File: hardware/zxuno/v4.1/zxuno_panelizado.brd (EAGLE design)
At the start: 103 parts, among them T1 BC846, U1 6SLX9TQG144, U2 FLASH-SPI-25XXSMD1, U4 AD724, U5 50MHz, U6 3.3V, U7 1.2V, Y1 3.58M, Y2 4.43M

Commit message: Replico el circuito por 4 wire 0 (0 0) (190 0) (190 150) (0 150) (0 0) wire 0 (0 10) (190 10) wire 0 (0 140) (190 140)
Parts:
- added AUDIO1, AUDIO2, AUDIO3: Audio, SparkFun-Connectors:AUDIO-JACK
- added C100, C101, C107, C108, C132, C133, C134, C135, C136, C137, C143, C144, C60, C61, C62, C63, C64, C65, C71, C72, C96, C97, C98, C99: 10uF, rcl:C0805
- added C102, C103, C104, C109, C110, C111, C112, C113, C114, C115, C116, C117, C118, C119, C120, C121, C122, C123, C124, C125, C126, C127, C129, C138, C139, C140, C37, C38, C39, C40, C41, C42, C43, C44, C45, C46, C47, C48, C49, C50, C51, C52, C53, C54, C55, C57, C66, C67, C68, C73, C74, C75, C76, C77, C78, C79, C80, C81, C82, C83, C84, C85, C86, C87, C88, C89, C90, C91, C93: 100nF, rcl:C0603
- added C105, C141, C69: 7.5pF, rcl:C0805
- added C106, C142, C70: 220uF, rcl:153CLV-0605
- added C128, C130, C131, C56, C58, C59, C92, C94, C95: 10nF, rcl:C0805
- added CVBS1, CVBS2, CVBS3: RCA, uzebox:RCA
- added D10, D13, D14, D15, D18, D19, D20, D8, D9: (no value), adafruit:SOD-323F
- added D11, D12, D16, D17, D6, D7: (no value), led:CHIP-LED0805
- added EAR1, EAR2, EAR3: EAR, SparkFun-Connectors:AUDIO-JACK
- added H2, H3, H4: MOUNT-HOLE2.8, holes:2,8
- added J1, J13, J14, J2, J3, J5, J6, J7, J9: (no value), pinhead:1X12
- added J15, J4, J8: (no value), pinhead:2X02
- added JOY1, JOY2, JOY3: (no value), SparkFun-Connectors:DB9_MALE
- added JTAG1, JTAG2, JTAG3: JTAG, con-molex:53047-06
- added L10, L11, L12, L4, L5, L6, L7, L8, L9: (no value), rcl:M0805
- added PS/1, PS/3, PS/4: PS/2 Keyb, ZX_UNO_0_14:DINC/MIN_TM/6_1PRIMARY
- added PWCON1, PWCON2, PWCON3, RST1, RST2, RST3, SW1, SW2, SW3: (no value), pinhead:1X02
- added PWUSB1, PWUSB2, PWUSB3: MICROUSB, zxuno_rev_mcleod:MICRO_USB_1PRIMARY
- added R100, R104, R109, R110, R113, R116, R121, R122, R33, R34, R35, R36, R40, R45, R46, R49, R52, R57, R58, R65, R66, R67, R68, R72, R77, R78, R81, R84, R89, R90, R97, R98, R99: 510, rcl:M0805
- added R101, R106, R107, R112, R115, R118, R37, R42, R43, R48, R51, R54, R69, R74, R75, R80, R83, R86: 2K, rcl:M0805
- added R102, R103, R105, R108, R119, R120, R127, R128, R38, R39, R41, R44, R55, R56, R63, R64, R70, R71, R73, R76, R87, R88, R95, R96: 10K, rcl:M0805
- added R111, R114, R117, R47, R50, R53, R79, R82, R85: 1K, rcl:M0805
- added R123, R124, R125, R126, R59, R60, R61, R62, R91, R92, R93, R94: 75, rcl:M0805
- added RGB1, RGB2, RGB3: RGB, con-molex:53048-09
- added SDCARD1, SDCARD2, SDCARD3: (no value), zxuno_rev_mcleod:SDCMF-10915W010
- added T2, T3, T4: BC846, transistor:SOT23
- added U10, U17, U24: FLASH-SPI-25XXSMD1, GadgetFactory:SO08-EIAJ
- added U11, U18, U25: 3.3V, burr-brown:SOT223
- added U12, U19, U26: 1.2V, burr-brown:SOT223
- added U13, U20, U27: AD724, ad725:SO16W
- added U14, U21, U28: 50MHz, ZX_UNO_0_15:SM/OSC_1PRIMARY
- added U15, U22, U8: 6SLX9TQG144, xilinx_devices_V6:TQ144
- added U16, U23, U9: (no value), GadgetFactory:TSOP44-II
- added Y3, Y5, Y7: 3.58M, crystal:HC49UP
- added Y4, Y6, Y8: 4.43M, crystal:HC49UP
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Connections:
- new net 1.2V1: C39.2, C40.2, C41.2, C42.2, C43.2, L6.2, U8.P128, U8.P19, U8.P28, U8.P52, U8.P89
- new net 1.2V2: C75.2, C76.2, C77.2, C78.2, C79.2, L9.2, U15.P128, U15.P19, U15.P28, U15.P52, U15.P89
- new net 1.2V3: C111.2, C112.2, C113.2, C114.2, C115.2, L12.2, U22.P128, U22.P19, U22.P28, U22.P52, U22.P89
- new net 3.3V1: C37.1, C38.2, C44.2, C45.2, C46.2, C47.2, C48.2, C49.2, C50.2, C51.2, C52.2, C53.2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
- new net 3.3V2: C73.1, C74.2, C80.2, C81.2, C82.2, C83.2, C84.2, C85.2, C86.2, C87.2, C88.2, C89.2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
- new net 3.3V3: C109.1, C110.2, C116.2, C117.2, C118.2, C119.2, C120.2, C121.2, C122.2, C123.2, C124.2, C125.2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
- new net 5V1: C62.1, C64.1, C71.2, C72.2, J1.1, L4.2, PS/1.4, R45.1, R58.2, U11.3, U12.3, U13.14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
- new net 5V2: C100.1, C107.2, C108.2, C98.1, J5.1, L7.2, PS/3.4, R77.1, R90.2, U18.3, U19.3, U20.14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
- new net 5V3: C134.1, C136.1, C143.2, C144.2, J9.1, L10.2, PS/4.4, R109.1, R122.2, U25.3, U26.3, U27.14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
- new net AUDIO_LEFT1: R42.2, U8.P10
- new net AUDIO_LEFT2: R74.2, U15.P10
- new net AUDIO_LEFT3: R106.2, U22.P10
- new net AUDIO_RIGHT1: R43.2, U8.P9
- new net AUDIO_RIGHT2: R75.2, U15.P9
- new net AUDIO_RIGHT3: R107.2, U22.P9
- new net B10: C104.2, R84.1, R85.1, R86.1, R93.1, RGB2.7
- new net B11: R118.2, U22.P88
- new net B12: R117.2, U22.P92
- new net B13: R116.2, U22.P93
- new net B14: C140.2, R116.1, R117.1, R118.1, R125.1, RGB3.7
- new net B3: R54.2, U8.P88
- new net B4: R53.2, U8.P92
- new net B5: R52.2, U8.P93
- new net B6: C68.2, R52.1, R53.1, R54.1, R61.1, RGB1.7
- new net B7: R86.2, U15.P88
- new net B8: R85.2, U15.P92
- new net B9: R84.2, U15.P93
- new net CLK1: U14.3, U8.P55
- new net CLK2: U15.P55, U21.3
- new net CLK3: U22.P55, U28.3
- new net CSYNC1: RGB1.3, U13.16, U8.P87
- new net CSYNC2: RGB2.3, U15.P87, U20.16
- new net CSYNC3: RGB3.3, U22.P87, U27.16
- new net EAR1: R38.1, T2.3, U8.P94
- new net EAR2: R70.1, T3.3, U15.P94
- new net EAR3: R102.1, T4.3, U22.P94
- new net EXT1: J1.2, U8.P57
- new net EXT100: J9.5, U22.P43
- new net EXT101: J13.5, U22.P41
- new net EXT102: J14.5, U22.P40
- new net EXT103: J9.6, U22.P35
- new net EXT104: J13.6, U22.P34
- new net EXT105: J14.6, U22.P33
- new net EXT106: J9.7, U22.P32
- new net EXT107: J13.7, U22.P30
- new net EXT108: J14.7, U22.P29
- new net EXT109: J9.8, U22.P27
- new net EXT110: J13.8, U22.P26
- new net EXT111: J14.8, U22.P24
- new net EXT112: J9.9, U22.P23
- new net EXT113: J13.9, U22.P22
- new net EXT114: J14.9, U22.P21
- new net EXT115: J9.10, U22.P17
- new net EXT116: J13.10, U22.P16
- new net EXT117: J14.10, U22.P15
- new net EXT118: J9.11, U22.P14
- new net EXT119: J13.11, U22.P12
- new net EXT120: J14.1, U22.P58
- new net EXT2: J2.2, U8.P56
- new net EXT3: J3.2, U8.P51
- new net EXT36: J3.3, U8.P47
- new net EXT37: J1.4, U8.P46
- new net EXT38: J2.4, U8.P45
- new net EXT39: J3.4, U8.P44
- new net EXT4: J1.3, U8.P50
- new net EXT40: J1.5, U8.P43
- new net EXT41: J2.5, U8.P41
- new net EXT42: J3.5, U8.P40
- new net EXT43: J1.6, U8.P35
- new net EXT44: J2.6, U8.P34
- new net EXT45: J3.6, U8.P33
- new net EXT46: J1.7, U8.P32
- new net EXT47: J2.7, U8.P30
- new net EXT48: J3.7, U8.P29
- new net EXT49: J1.8, U8.P27
- new net EXT5: J2.3, U8.P48
- new net EXT50: J2.8, U8.P26
- new net EXT51: J3.8, U8.P24
- new net EXT52: J1.9, U8.P23
- new net EXT53: J2.9, U8.P22
- new net EXT54: J3.9, U8.P21
- new net EXT55: J1.10, U8.P17
- new net EXT56: J2.10, U8.P16
- new net EXT57: J3.10, U8.P15
- new net EXT58: J1.11, U8.P14
- new net EXT59: J2.11, U8.P12
- new net EXT60: J3.1, U8.P58
- new net EXT61: J5.2, U15.P57
- new net EXT62: J6.2, U15.P56
- new net EXT63: J7.2, U15.P51
- new net EXT64: J5.3, U15.P50
- new net EXT65: J6.3, U15.P48
- new net EXT66: J7.3, U15.P47
- new net EXT67: J5.4, U15.P46
- new net EXT68: J6.4, U15.P45
- new net EXT69: J7.4, U15.P44
- new net EXT70: J5.5, U15.P43
- new net EXT71: J6.5, U15.P41
- new net EXT72: J7.5, U15.P40
- new net EXT73: J5.6, U15.P35
- new net EXT74: J6.6, U15.P34
- new net EXT75: J7.6, U15.P33
- new net EXT76: J5.7, U15.P32
- new net EXT77: J6.7, U15.P30
- new net EXT78: J7.7, U15.P29
- new net EXT79: J5.8, U15.P27
- new net EXT80: J6.8, U15.P26
- new net EXT81: J7.8, U15.P24
- new net EXT82: J5.9, U15.P23
- new net EXT83: J6.9, U15.P22
- new net EXT84: J7.9, U15.P21
- new net EXT85: J5.10, U15.P17
- new net EXT86: J6.10, U15.P16
- new net EXT87: J7.10, U15.P15
- new net EXT88: J5.11, U15.P14
- new net EXT89: J6.11, U15.P12
- new net EXT90: J7.1, U15.P58
- new net EXT91: J9.2, U22.P57
- new net EXT92: J13.2, U22.P56
- new net EXT93: J14.2, U22.P51
- new net EXT94: J9.3, U22.P50
- new net EXT95: J13.3, U22.P48
- new net EXT96: J14.3, U22.P47
- new net EXT97: J9.4, U22.P46
- new net EXT98: J13.4, U22.P45
- new net EXT99: J14.4, U22.P44
- new net FLASH_CS1: U10.1, U8.P38
- new net FLASH_CS2: U15.P38, U17.1
- new net FLASH_CS3: U22.P38, U24.1
- new net FLASH_HOLD1: U10.7, U8.P61
- new net FLASH_HOLD2: U15.P61, U17.7
- new net FLASH_HOLD3: U22.P61, U24.7
- new net FLASH_MISO1: U10.2, U8.P65
- new net FLASH_MISO2: U15.P65, U17.2
- new net FLASH_MISO3: U22.P65, U24.2
- new net FLASH_MOSI1: U10.5, U8.P64
- new net FLASH_MOSI2: U15.P64, U17.5
- new net FLASH_MOSI3: U22.P64, U24.5
- new net FLASH_SCK1: U10.6, U8.P70
- new net FLASH_SCK2: U15.P70, U17.6
- new net FLASH_SCK3: U22.P70, U24.6
- new net FLASH_WP1: U10.3, U8.P62
- new net FLASH_WP2: U15.P62, U17.3
- new net FLASH_WP3: U22.P62, U24.3
- new net G10: C103.2, R81.1, R82.1, R83.1, R92.1, RGB2.6
- new net G11: R115.2, U22.P82
- new net G12: R114.2, U22.P83
- new net G13: R113.2, U22.P84
- new net G14: C139.2, R113.1, R114.1, R115.1, R124.1, RGB3.6
- new net G3: R51.2, U8.P82
- new net G4: R50.2, U8.P83
- new net G5: R49.2, U8.P84
- new net G6: C67.2, R49.1, R50.1, R51.1, R60.1, RGB1.6
- new net G7: R83.2, U15.P82
- new net G8: R82.2, U15.P83
- new net G9: R81.2, U15.P84
- new net GND1: AUDIO1.SLEEVE, C37.2, C38.1, C39.1, C40.1, C41.1, C42.1, C43.1, C44.1, C45.1, C46.1, C47.1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
- new net GND2: AUDIO2.SLEEVE, C100.2, C101.2, C105.2, C107.1, C108.1, C73.2, C74.1, C75.1, C76.1, C77.1, C78.1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
- new net GND3: AUDIO3.SLEEVE, C109.2, C110.1, C111.1, C112.1, C113.1, C114.1, C115.1, C116.1, C117.1, C118.1, C119.1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
- new net JOY_DOWN1: JOY1.2, U8.P5
- new net JOY_DOWN2: JOY2.2, U15.P5
- new net JOY_DOWN3: JOY3.2, U22.P5
- new net JOY_FIRE10: JOY3.6, U22.P2
- new net JOY_FIRE11: JOY3.9, U22.P8
- new net JOY_FIRE12: J15.1, U22.P39
- new net JOY_FIRE4: JOY1.6, U8.P2
- new net JOY_FIRE5: JOY1.9, U8.P8
- new net JOY_FIRE6: J4.1, U8.P39
- new net JOY_FIRE7: JOY2.6, U15.P2
- new net JOY_FIRE8: JOY2.9, U15.P8
- new net JOY_FIRE9: J8.1, U15.P39
- new net JOY_LEFT1: JOY1.3, U8.P6
- new net JOY_LEFT2: JOY2.3, U15.P6
- new net JOY_LEFT3: JOY3.3, U22.P6
- new net JOY_RIGHT1: JOY1.4, U8.P7
- new net JOY_RIGHT2: JOY2.4, U15.P7
- new net JOY_RIGHT3: JOY3.4, U22.P7
- new net JOY_UP1: JOY1.1, U8.P1
- new net JOY_UP2: JOY2.1, U15.P1
- new net JOY_UP3: JOY3.1, U22.P1
- new net L-OUT1: AUDIO1.TIP, C60.2, RGB1.9
- new net L-OUT2: AUDIO2.TIP, C96.2, RGB2.9
- new net L-OUT3: AUDIO3.TIP, C132.2, RGB3.9
- new net LED1: R57.2, U8.P11
- new net LED2: R89.2, U15.P11
- new net LED3: R121.2, U22.P11
- new net N$100: C135.1, L11.1, U25.2
- new net N$101: C137.1, L12.1, U26.2
- new net N$102: C139.1, U27.7
- new net N$103: C138.1, U27.6
- new net N$104: C141.1, U27.3, Y7.2, Y8.2
- new net N$105: D20.A, R120.1, Y8.1
- new net N$106: D19.A, R119.2, Y7.1
- new net N$107: C142.+, U27.10
- new net N$108: C140.1, U27.8
- new net N$109: C142.-, R126.1
- new net N$110: CVBS3.SIG, R126.2
- new net N$111: D16.A, R121.1
- new net N$112: D17.A, R122.1
- new net N$113: R101.1, RST3.2, U22.P37
- new net N$114: R127.1, SDCARD3.8
- new net N$115: R128.1, SDCARD3.9
- new net N$116: J15.4, R109.2
- new net N$16: PS/1.6, R33.1
- new net N$29: PS/1.5, R34.1
- new net N$30: PS/1.2, R35.1
- new net N$33: PS/1.1, R36.1
- new net N$34: R39.2, T2.1
- new net N$35: C56.1, C57.1, D8.C, R39.1
- new net N$36: C57.2, R40.2
- new net N$37: EAR1.TIP, R40.1, R41.1
- new net N$38: C58.1, C61.1, R43.1
- new net N$39: C59.1, C60.1, R42.1
- new net N$40: PWCON1.2, PWUSB1.1, SW1.2
- new net N$41: L4.1, SW1.1
- new net N$42: C63.1, L5.1, U11.2
- new net N$43: C65.1, L6.1, U12.2
- new net N$44: C67.1, U13.7
- new net N$45: C66.1, U13.6
- new net N$46: C69.1, U13.3, Y3.2, Y4.2
- new net N$47: D10.A, R56.1, Y4.1
- new net N$48: D9.A, R55.2, Y3.1
- new net N$49: C70.+, U13.10
- new net N$50: C68.1, U13.8
- new net N$51: C70.-, R62.1
- new net N$52: CVBS1.SIG, R62.2
- new net N$53: D6.A, R57.1
- new net N$54: D7.A, R58.1
- new net N$55: R37.1, RST1.2, U8.P37
- new net N$56: R63.1, SDCARD1.8
- new net N$57: R64.1, SDCARD1.9
- new net N$58: J4.4, R45.2
- new net N$59: PS/3.6, R65.1
- new net N$60: PS/3.5, R66.1
- new net N$61: PS/3.2, R67.1
- new net N$62: PS/3.1, R68.1
- new net N$63: R71.2, T3.1
- new net N$64: C92.1, C93.1, D13.C, R71.1
- new net N$65: C93.2, R72.2
- new net N$66: EAR2.TIP, R72.1, R73.1
- new net N$67: C94.1, C97.1, R75.1
- new net N$68: C95.1, C96.1, R74.1
- new net N$69: PWCON2.2, PWUSB2.1, SW2.2
- new net N$70: L7.1, SW2.1
- new net N$71: C99.1, L8.1, U18.2
- new net N$72: C101.1, L9.1, U19.2
- new net N$73: C103.1, U20.7
- new net N$74: C102.1, U20.6
- new net N$75: C105.1, U20.3, Y5.2, Y6.2
- new net N$76: D15.A, R88.1, Y6.1
- new net N$77: D14.A, R87.2, Y5.1
- new net N$78: C106.+, U20.10
- new net N$79: C104.1, U20.8
- new net N$80: C106.-, R94.1
- new net N$81: CVBS2.SIG, R94.2
- new net N$82: D11.A, R89.1
- new net N$83: D12.A, R90.1
- new net N$84: R69.1, RST2.2, U15.P37
- new net N$85: R95.1, SDCARD2.8
- new net N$86: R96.1, SDCARD2.9
- new net N$87: J8.4, R77.2
- new net N$88: PS/4.6, R97.1
- new net N$89: PS/4.5, R98.1
- new net N$90: PS/4.2, R99.1
- new net N$91: PS/4.1, R100.1
- new net N$92: R103.2, T4.1
- new net N$93: C128.1, C129.1, D18.C, R103.1
- new net N$94: C129.2, R104.2
- new net N$95: EAR3.TIP, R104.1, R105.1
- new net N$96: C130.1, C133.1, R107.1
- new net N$97: C131.1, C132.1, R106.1
- new net N$98: PWCON3.2, PWUSB3.1, SW3.2
- new net N$99: L10.1, SW3.1
- new net PIN1: J4.3, JOY1.7
- new net PIN2: J4.2, JOY1.5
- new net PIN3: J8.3, JOY2.7
- new net PIN4: J8.2, JOY2.5
- new net PIN6: J15.3, JOY3.7
- new net PIN8: J15.2, JOY3.5
- new net PS2_CLK1: R34.2, U8.P99
- new net PS2_CLK2: R66.2, U15.P99
- new net PS2_CLK3: R98.2, U22.P99
- new net PS2_DATA1: R36.2, U8.P98
- new net PS2_DATA2: R68.2, U15.P98
- new net PS2_DATA3: R100.2, U22.P98
- new net PS2_PIN1: R33.2, U8.P95
- new net PS2_PIN3: R35.2, U8.P97
- new net PS2_PIN4: R65.2, U15.P95
- new net PS2_PIN5: R67.2, U15.P97
- new net PS2_PIN7: R97.2, U22.P95
- new net PS2_PIN8: R99.2, U22.P97
- new net R-OUT1: AUDIO1.RING, C61.2, RGB1.8
- new net R-OUT2: AUDIO2.RING, C97.2, RGB2.8
- new net R-OUT3: AUDIO3.RING, C133.2, RGB3.8
- new net R10: C102.2, R78.1, R79.1, R80.1, R91.1, RGB2.5
- new net R11: R112.2, U22.P79
- new net R12: R111.2, U22.P80
- new net R13: R110.2, U22.P81
- new net R14: C138.2, R110.1, R111.1, R112.1, R123.1, RGB3.5
- new net R3: R48.2, U8.P79
- new net R4: R47.2, U8.P80
- new net R5: R46.2, U8.P81
- new net R6: C66.2, R46.1, R47.1, R48.1, R59.1, RGB1.5
- new net R7: R80.2, U15.P79
- new net R8: R79.2, U15.P80
- new net R9: R78.2, U15.P81
- new net SD_CS1: SDCARD1.1, U8.P59
- new net SD_CS2: SDCARD2.1, U15.P59
- new net SD_CS3: SDCARD3.1, U22.P59
- new net SD_MISO1: R44.2, SDCARD1.7, U8.P78
- new net SD_MISO2: R76.2, SDCARD2.7, U15.P78
- new net SD_MISO3: R108.2, SDCARD3.7, U22.P78
- new net SD_MOSI1: SDCARD1.2, U8.P74
- new net SD_MOSI2: SDCARD2.2, U15.P74
- new net SD_MOSI3: SDCARD3.2, U22.P74
- new net SD_SCK1: SDCARD1.5, U8.P75
- new net SD_SCK2: SDCARD2.5, U15.P75
- new net SD_SCK3: SDCARD3.5, U22.P75
- new net STDN1: R55.1, U13.1, U8.P66
- new net STDN2: R87.1, U15.P66, U20.1
- new net STDN3: R119.1, U22.P66, U27.1
- new net STDNB1: R56.2, U8.P67
- new net STDNB2: R88.2, U15.P67
- new net STDNB3: R120.2, U22.P67
- new net TCK1: JTAG1.3, U8.P109
- new net TCK2: JTAG2.3, U15.P109
- new net TCK3: JTAG3.3, U22.P109
- new net TDI1: JTAG1.5, U8.P110
- new net TDI2: JTAG2.5, U15.P110
- new net TDI3: JTAG3.5, U22.P110
- new net TDO1: JTAG1.4, U8.P106
- new net TDO2: JTAG2.4, U15.P106
- new net TDO3: JTAG3.4, U22.P106
- new net TMS1: JTAG1.6, U8.P107
- new net TMS2: JTAG2.6, U15.P107
- new net TMS3: JTAG3.6, U22.P107
- new net VSYNC1: RGB1.2, U8.P85
- new net VSYNC2: RGB2.2, U15.P85
- new net VSYNC3: RGB3.2, U22.P85
- new net WR1: U8.P121, U9.15
- new net WR2: U15.P121, U16.15
- new net WR3: U22.P121, U23.15
- new net XA21: U8.P141, U9.3
- new net XA22: U8.P137, U9.5
- new net XA23: U8.P134, U9.6
- new net XA24: U8.P133, U9.7
- new net XA25: U8.P120, U9.16
- new net XA26: U8.P118, U9.17
- new net XA27: U8.P116, U9.18
- new net XA28: U8.P114, U9.19
- new net XA29: U8.P112, U9.20
- new net XA30: U8.P104, U9.26
- new net XA31: U8.P102, U9.27
- new net XA32: U8.P101, U9.28
- new net XA33: U8.P100, U9.29
- new net XA34: U8.P111, U9.30
- new net XA35: U8.P131, U9.38
- new net XA36: U8.P138, U9.39
- new net XA37: U8.P140, U9.40
- new net XA38: U8.P142, U9.41
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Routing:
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- added copper zone on layer 1, net GND1
- added copper zone on layer 16, net GND1
- added copper zone on layer 1, net GND2
- added copper zone on layer 16, net GND2
- added copper zone on layer 1, net GND3
- added copper zone on layer 16, net GND3
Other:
- board outline added: 190 x 150 mm

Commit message: wire 0 (0 66) (190 66) wire 0 (0 84) (190 84) wire 0 (86 10) (86 140) wire 0 (104 10) (104 140)
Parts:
- moved AUDIO2 0.06 mm to (169.4, 136.4)
- moved D11 0.06 mm to (185.3, 138.4)
- moved H3 0.06 mm to (141.0, 136.0)
- moved J7 0.06 mm to (121.2, 138.0)
- moved R89 0.06 mm to (179.8, 138.4)
- moved C101 0.06 mm to (117.6, 108.8)
- moved C103 0.06 mm to (135.0, 96.8)
- moved C73 0.06 mm to (175.2, 114.1)
- moved C74 0.06 mm to (123.1, 111.0)
- moved C75 0.06 mm to (141.2, 123.6)
- moved C76 0.06 mm to (148.1, 123.6)
- moved C77 0.06 mm to (155.1, 115.5)
- moved C79 0.06 mm to (136.5, 117.0)
- moved C80 0.06 mm to (144.3, 123.6)
- moved C81 0.06 mm to (153.3, 123.6)
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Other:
- outline, holes or cut-outs redrawn

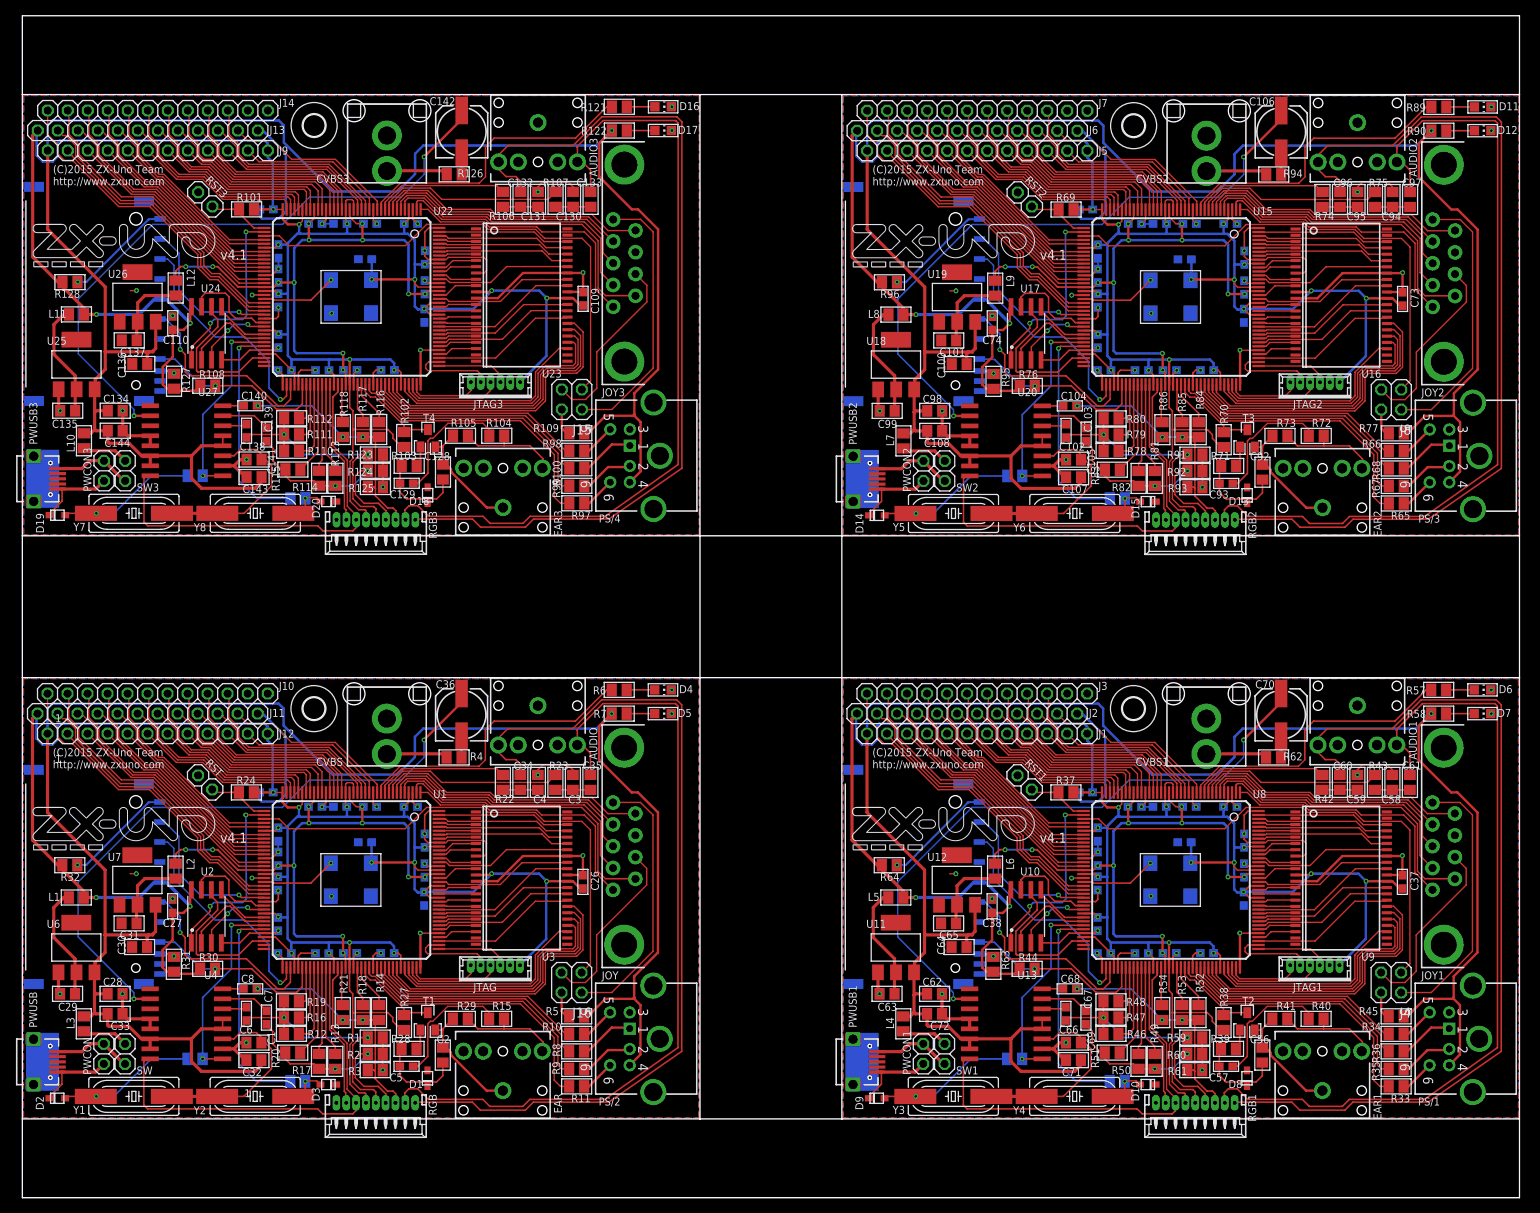
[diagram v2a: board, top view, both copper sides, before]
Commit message: Añado fiduciales y borro esquemático panelizado
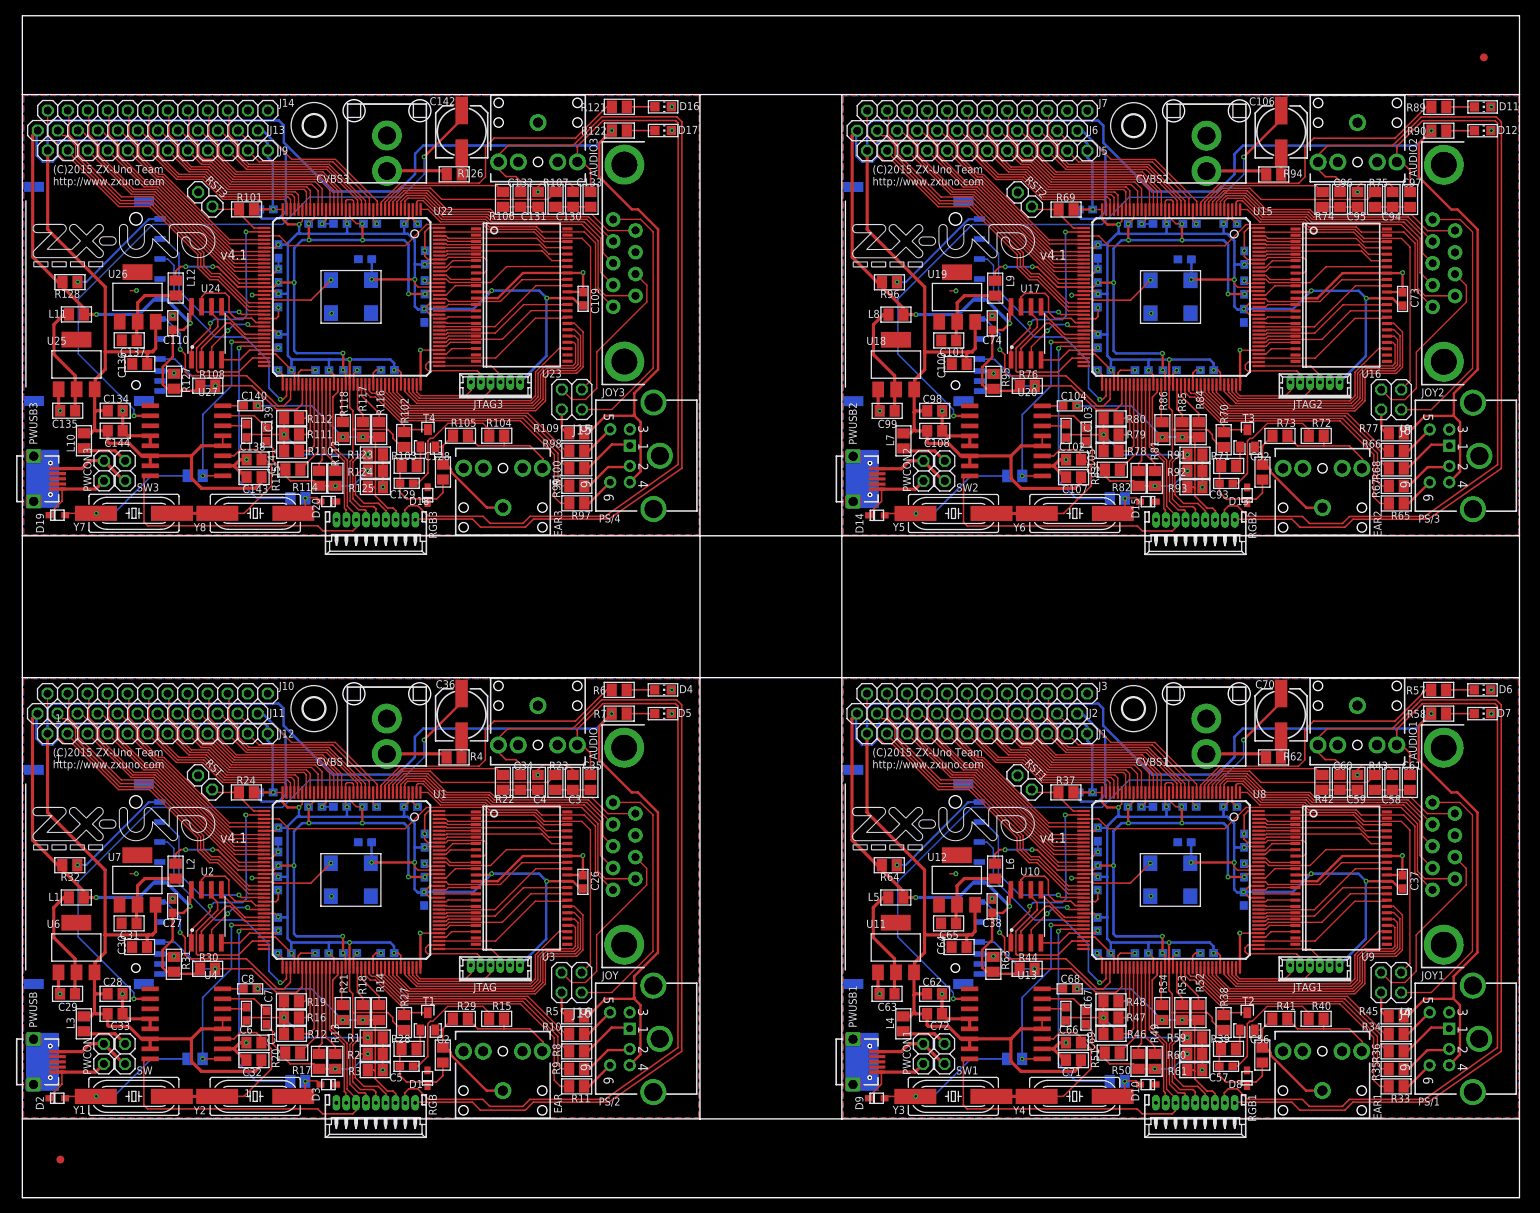
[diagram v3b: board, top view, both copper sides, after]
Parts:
- added E$1, E$2: (no value), adafruit:FIDUCIAL_1MM
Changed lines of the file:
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@@
 <attribute name="NAME" x="37.30625" y="128.80578125" size="1.016" layer="25" font="vector" ratio="15"/>
 </element>
+<element name="E$1" library="adafruit" package="FIDUCIAL_1MM" value="" x="4.82203125" y="4.841875"/>
+<element name="E$2" library="adafruit" package="FIDUCIAL_1MM" value="" x="185.47953125" y="144.72046875"/>
 </elements>
 <signals>

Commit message: Vacío panelizado
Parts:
- removed AUDIO, AUDIO1, AUDIO2, AUDIO3: Audio, SparkFun-Connectors:AUDIO-JACK
- removed C1, C105, C141, C69: 7.5pF, rcl:C0805
- removed C10, C102, C103, C104, C109, C11, C110, C111, C112, C113, C114, C115, C116, C117, C118, C119, C12, C120, C121, C122, C123, C124, C125, C126, C127, C129, C13, C138, C139, C14, C140, C15, C16, C17, C18, C19, C20, C21, C22, C23, C24, C25, C26, C27, C37, C38, C39, C40, C41, C42, C43, C44, C45, C46, C47, C48, C49, C5, C50, C51, C52, C53, C54, C55, C57, C6, C66, C67, C68, C7, C73, C74, C75, C76, C77, C78, C79, C8, C80, C81, C82, C83, C84, C85, C86, C87, C88, C89, C9, C90, C91, C93: 100nF, rcl:C0603
- removed C100, C101, C107, C108, C132, C133, C134, C135, C136, C137, C143, C144, C28, C29, C30, C31, C32, C33, C34, C35, C60, C61, C62, C63, C64, C65, C71, C72, C96, C97, C98, C99: 10uF, rcl:C0805
- removed C106, C142, C36, C70: 220uF, rcl:153CLV-0605
- removed C128, C130, C131, C2, C3, C4, C56, C58, C59, C92, C94, C95: 10nF, rcl:C0805
- removed CVBS, CVBS1, CVBS2, CVBS3: RCA, uzebox:RCA
- removed D1, D10, D13, D14, D15, D18, D19, D2, D20, D3, D8, D9: (no value), adafruit:SOD-323F
- removed D11, D12, D16, D17, D4, D5, D6, D7: (no value), led:CHIP-LED0805
- removed EAR, EAR1, EAR2, EAR3: EAR, SparkFun-Connectors:AUDIO-JACK
- removed H1, H2, H3, H4: MOUNT-HOLE2.8, holes:2,8
- removed J1, J10, J11, J12, J13, J14, J2, J3, J5, J6, J7, J9: (no value), pinhead:1X12
- removed J15, J16, J4, J8: (no value), pinhead:2X02
- removed JOY, JOY1, JOY2, JOY3: (no value), SparkFun-Connectors:DB9_MALE
- removed JTAG, JTAG1, JTAG2, JTAG3: JTAG, con-molex:53047-06
- removed L1, L10, L11, L12, L2, L3, L4, L5, L6, L7, L8, L9: (no value), rcl:M0805
- removed PS/1, PS/2, PS/3, PS/4: PS/2 Keyb, ZX_UNO_0_14:DINC/MIN_TM/6_1PRIMARY
- removed PWCON, PWCON1, PWCON2, PWCON3, RST, RST1, RST2, RST3, SW, SW1, SW2, SW3: (no value), pinhead:1X02
- removed PWUSB, PWUSB1, PWUSB2, PWUSB3: MICROUSB, zxuno_rev_mcleod:MICRO_USB_1PRIMARY
- removed R1, R123, R124, R125, R126, R2, R3, R4, R59, R60, R61, R62, R91, R92, R93, R94: 75, rcl:M0805
- removed R10, R100, R104, R109, R11, R110, R113, R116, R12, R121, R122, R13, R14, R15, R33, R34, R35, R36, R40, R45, R46, R49, R5, R52, R57, R58, R6, R65, R66, R67, R68, R7, R72, R77, R78, R8, R81, R84, R89, R9, R90, R97, R98, R99: 510, rcl:M0805
- removed R101, R106, R107, R112, R115, R118, R19, R20, R21, R22, R23, R24, R37, R42, R43, R48, R51, R54, R69, R74, R75, R80, R83, R86: 2K, rcl:M0805
- removed R102, R103, R105, R108, R119, R120, R127, R128, R25, R26, R27, R28, R29, R30, R31, R32, R38, R39, R41, R44, R55, R56, R63, R64, R70, R71, R73, R76, R87, R88, R95, R96: 10K, rcl:M0805
- removed R111, R114, R117, R16, R17, R18, R47, R50, R53, R79, R82, R85: 1K, rcl:M0805
- removed RGB, RGB1, RGB2, RGB3: RGB, con-molex:53048-09
- removed SDCARD, SDCARD1, SDCARD2, SDCARD3: (no value), zxuno_rev_mcleod:SDCMF-10915W010
- removed T1, T2, T3, T4: BC846, transistor:SOT23
- removed U1, U15, U22, U8: 6SLX9TQG144, xilinx_devices_V6:TQ144
- removed U10, U17, U2, U24: FLASH-SPI-25XXSMD1, GadgetFactory:SO08-EIAJ
- removed U11, U18, U25, U6: 3.3V, burr-brown:SOT223
- removed U12, U19, U26, U7: 1.2V, burr-brown:SOT223
- removed U13, U20, U27, U4: AD724, ad725:SO16W
- removed U14, U21, U28, U5: 50MHz, ZX_UNO_0_15:SM/OSC_1PRIMARY
- removed U16, U23, U3, U9: (no value), GadgetFactory:TSOP44-II
- removed Y1, Y3, Y5, Y7: 3.58M, crystal:HC49UP
- removed Y2, Y4, Y6, Y8: 4.43M, crystal:HC49UP
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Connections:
- removed net 1.2V: C10.2, C11.2, C12.2, C13.2, C9.2, L2.2, U1.P128, U1.P19, U1.P28, U1.P52, U1.P89
- removed net 1.2V1: C39.2, C40.2, C41.2, C42.2, C43.2, L6.2, U8.P128, U8.P19, U8.P28, U8.P52, U8.P89
- removed net 1.2V2: C75.2, C76.2, C77.2, C78.2, C79.2, L9.2, U15.P128, U15.P19, U15.P28, U15.P52, U15.P89
- removed net 1.2V3: C111.2, C112.2, C113.2, C114.2, C115.2, L12.2, U22.P128, U22.P19, U22.P28, U22.P52, U22.P89
- removed net 3.3V: C14.2, C15.2, C16.2, C17.2, C18.2, C19.2, C20.2, C21.2, C22.2, C23.2, C24.2, C25.2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
- removed net 3.3V1: C37.1, C38.2, C44.2, C45.2, C46.2, C47.2, C48.2, C49.2, C50.2, C51.2, C52.2, C53.2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
- removed net 3.3V2: C73.1, C74.2, C80.2, C81.2, C82.2, C83.2, C84.2, C85.2, C86.2, C87.2, C88.2, C89.2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
- removed net 3.3V3: C109.1, C110.2, C116.2, C117.2, C118.2, C119.2, C120.2, C121.2, C122.2, C123.2, C124.2, C125.2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
- removed net 5V: C28.1, C30.1, C32.2, C33.2, J12.1, L3.2, PS/2.4, R5.1, R7.2, U4.14, U4.15, U4.4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
- removed net 5V1: C62.1, C64.1, C71.2, C72.2, J1.1, L4.2, PS/1.4, R45.1, R58.2, U11.3, U12.3, U13.14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
- removed net 5V2: C100.1, C107.2, C108.2, C98.1, J5.1, L7.2, PS/3.4, R77.1, R90.2, U18.3, U19.3, U20.14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
- removed net 5V3: C134.1, C136.1, C143.2, C144.2, J9.1, L10.2, PS/4.4, R109.1, R122.2, U25.3, U26.3, U27.14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
- removed net AUDIO_LEFT: R22.2, U1.P10
- removed net AUDIO_LEFT1: R42.2, U8.P10
- removed net AUDIO_LEFT2: R74.2, U15.P10
- removed net AUDIO_LEFT3: R106.2, U22.P10
- removed net AUDIO_RIGHT: R23.2, U1.P9
- removed net AUDIO_RIGHT1: R43.2, U8.P9
- removed net AUDIO_RIGHT2: R75.2, U15.P9
- removed net AUDIO_RIGHT3: R107.2, U22.P9
- removed net B: C8.2, R14.1, R18.1, R21.1, R3.1, RGB.7
- removed net B0: R21.2, U1.P88
- removed net B1: R18.2, U1.P92
- removed net B10: C104.2, R84.1, R85.1, R86.1, R93.1, RGB2.7
- removed net B11: R118.2, U22.P88
- removed net B12: R117.2, U22.P92
- removed net B13: R116.2, U22.P93
- removed net B14: C140.2, R116.1, R117.1, R118.1, R125.1, RGB3.7
- removed net B2: R14.2, U1.P93
- removed net B3: R54.2, U8.P88
- removed net B4: R53.2, U8.P92
- removed net B5: R52.2, U8.P93
- removed net B6: C68.2, R52.1, R53.1, R54.1, R61.1, RGB1.7
- removed net B7: R86.2, U15.P88
- removed net B8: R85.2, U15.P92
- removed net B9: R84.2, U15.P93
- removed net CLK: U1.P55, U5.3
- removed net CLK1: U14.3, U8.P55
- removed net CLK2: U15.P55, U21.3
- removed net CLK3: U22.P55, U28.3
- removed net CSYNC: RGB.3, U1.P87, U4.16
- removed net CSYNC1: RGB1.3, U13.16, U8.P87
- removed net CSYNC2: RGB2.3, U15.P87, U20.16
- removed net CSYNC3: RGB3.3, U22.P87, U27.16
- removed net EAR: R27.1, T1.3, U1.P94
- removed net EAR1: R38.1, T2.3, U8.P94
- removed net EAR2: R70.1, T3.3, U15.P94
- removed net EAR3: R102.1, T4.3, U22.P94
- removed net EXT1: J1.2, U8.P57
- removed net EXT10: J12.3, U1.P50
- removed net EXT100: J9.5, U22.P43
- removed net EXT101: J13.5, U22.P41
- removed net EXT102: J14.5, U22.P40
- removed net EXT103: J9.6, U22.P35
- removed net EXT104: J13.6, U22.P34
- removed net EXT105: J14.6, U22.P33
- removed net EXT106: J9.7, U22.P32
- removed net EXT107: J13.7, U22.P30
- removed net EXT108: J14.7, U22.P29
- removed net EXT109: J9.8, U22.P27
- removed net EXT11: J11.3, U1.P48
- removed net EXT110: J13.8, U22.P26
- removed net EXT111: J14.8, U22.P24
- removed net EXT112: J9.9, U22.P23
- removed net EXT113: J13.9, U22.P22
- removed net EXT114: J14.9, U22.P21
- removed net EXT115: J9.10, U22.P17
- removed net EXT116: J13.10, U22.P16
- removed net EXT117: J14.10, U22.P15
- removed net EXT118: J9.11, U22.P14
- removed net EXT119: J13.11, U22.P12
- removed net EXT12: J10.3, U1.P47
- removed net EXT120: J14.1, U22.P58
- removed net EXT13: J12.4, U1.P46
- removed net EXT14: J11.4, U1.P45
- removed net EXT15: J10.4, U1.P44
- removed net EXT16: J12.5, U1.P43
- removed net EXT17: J11.5, U1.P41
- removed net EXT18: J10.5, U1.P40
- removed net EXT19: J12.6, U1.P35
- removed net EXT2: J2.2, U8.P56
- removed net EXT20: J11.6, U1.P34
- removed net EXT21: J10.6, U1.P33
- removed net EXT22: J12.7, U1.P32
- removed net EXT23: J11.7, U1.P30
- removed net EXT24: J10.7, U1.P29
- removed net EXT25: J12.8, U1.P27
- removed net EXT26: J11.8, U1.P26
- removed net EXT27: J10.8, U1.P24
- removed net EXT28: J12.9, U1.P23
- removed net EXT29: J11.9, U1.P22
- removed net EXT3: J3.2, U8.P51
- removed net EXT30: J10.9, U1.P21
- removed net EXT31: J12.10, U1.P17
- removed net EXT32: J11.10, U1.P16
- removed net EXT33: J10.10, U1.P15
- removed net EXT34: J12.11, U1.P14
- removed net EXT35: J11.11, U1.P12
- removed net EXT36: J3.3, U8.P47
- removed net EXT37: J1.4, U8.P46
- removed net EXT38: J2.4, U8.P45
- removed net EXT39: J3.4, U8.P44
- removed net EXT4: J1.3, U8.P50
- removed net EXT40: J1.5, U8.P43
- removed net EXT41: J2.5, U8.P41
- removed net EXT42: J3.5, U8.P40
- removed net EXT43: J1.6, U8.P35
- removed net EXT44: J2.6, U8.P34
- removed net EXT45: J3.6, U8.P33
- removed net EXT46: J1.7, U8.P32
- removed net EXT47: J2.7, U8.P30
- removed net EXT48: J3.7, U8.P29
- removed net EXT49: J1.8, U8.P27
- removed net EXT5: J2.3, U8.P48
- removed net EXT50: J2.8, U8.P26
- removed net EXT51: J3.8, U8.P24
- removed net EXT52: J1.9, U8.P23
- removed net EXT53: J2.9, U8.P22
- removed net EXT54: J3.9, U8.P21
- removed net EXT55: J1.10, U8.P17
- removed net EXT56: J2.10, U8.P16
- removed net EXT57: J3.10, U8.P15
- removed net EXT58: J1.11, U8.P14
- removed net EXT59: J2.11, U8.P12
- removed net EXT6: J10.1, U1.P58
- removed net EXT60: J3.1, U8.P58
- removed net EXT61: J5.2, U15.P57
- removed net EXT62: J6.2, U15.P56
- removed net EXT63: J7.2, U15.P51
- removed net EXT64: J5.3, U15.P50
- removed net EXT65: J6.3, U15.P48
- removed net EXT66: J7.3, U15.P47
- removed net EXT67: J5.4, U15.P46
- removed net EXT68: J6.4, U15.P45
- removed net EXT69: J7.4, U15.P44
- removed net EXT7: J12.2, U1.P57
- removed net EXT70: J5.5, U15.P43
- removed net EXT71: J6.5, U15.P41
- removed net EXT72: J7.5, U15.P40
- removed net EXT73: J5.6, U15.P35
- removed net EXT74: J6.6, U15.P34
- removed net EXT75: J7.6, U15.P33
- removed net EXT76: J5.7, U15.P32
- removed net EXT77: J6.7, U15.P30
- removed net EXT78: J7.7, U15.P29
- removed net EXT79: J5.8, U15.P27
- removed net EXT8: J11.2, U1.P56
- removed net EXT80: J6.8, U15.P26
- removed net EXT81: J7.8, U15.P24
- removed net EXT82: J5.9, U15.P23
- removed net EXT83: J6.9, U15.P22
- removed net EXT84: J7.9, U15.P21
- removed net EXT85: J5.10, U15.P17
- removed net EXT86: J6.10, U15.P16
- removed net EXT87: J7.10, U15.P15
- removed net EXT88: J5.11, U15.P14
- removed net EXT89: J6.11, U15.P12
- removed net EXT9: J10.2, U1.P51
- removed net EXT90: J7.1, U15.P58
- removed net EXT91: J9.2, U22.P57
- removed net EXT92: J13.2, U22.P56
- removed net EXT93: J14.2, U22.P51
- removed net EXT94: J9.3, U22.P50
- removed net EXT95: J13.3, U22.P48
- removed net EXT96: J14.3, U22.P47
- removed net EXT97: J9.4, U22.P46
- removed net EXT98: J13.4, U22.P45
- removed net EXT99: J14.4, U22.P44
- removed net FLASH_CS: U1.P38, U2.1
- removed net FLASH_CS1: U10.1, U8.P38
- removed net FLASH_CS2: U15.P38, U17.1
- removed net FLASH_CS3: U22.P38, U24.1
- removed net FLASH_HOLD: U1.P61, U2.7
- removed net FLASH_HOLD1: U10.7, U8.P61
- removed net FLASH_HOLD2: U15.P61, U17.7
- removed net FLASH_HOLD3: U22.P61, U24.7
- removed net FLASH_MISO: U1.P65, U2.2
- removed net FLASH_MISO1: U10.2, U8.P65
- removed net FLASH_MISO2: U15.P65, U17.2
- removed net FLASH_MISO3: U22.P65, U24.2
- removed net FLASH_MOSI: U1.P64, U2.5
- removed net FLASH_MOSI1: U10.5, U8.P64
- removed net FLASH_MOSI2: U15.P64, U17.5
- removed net FLASH_MOSI3: U22.P64, U24.5
- removed net FLASH_SCK: U1.P70, U2.6
- removed net FLASH_SCK1: U10.6, U8.P70
- removed net FLASH_SCK2: U15.P70, U17.6
- removed net FLASH_SCK3: U22.P70, U24.6
- removed net FLASH_WP: U1.P62, U2.3
- removed net FLASH_WP1: U10.3, U8.P62
- removed net FLASH_WP2: U15.P62, U17.3
- removed net FLASH_WP3: U22.P62, U24.3
- removed net G: C7.2, R13.1, R17.1, R2.1, R20.1, RGB.6
- removed net G0: R20.2, U1.P82
- removed net G1: R17.2, U1.P83
- removed net G10: C103.2, R81.1, R82.1, R83.1, R92.1, RGB2.6
- removed net G11: R115.2, U22.P82
- removed net G12: R114.2, U22.P83
- removed net G13: R113.2, U22.P84
- removed net G14: C139.2, R113.1, R114.1, R115.1, R124.1, RGB3.6
- removed net G2: R13.2, U1.P84
- removed net G3: R51.2, U8.P82
- removed net G4: R50.2, U8.P83
- removed net G5: R49.2, U8.P84
- removed net G6: C67.2, R49.1, R50.1, R51.1, R60.1, RGB1.6
- removed net G7: R83.2, U15.P82
- removed net G8: R82.2, U15.P83
- removed net G9: R81.2, U15.P84
- removed net GND: AUDIO.SLEEVE, C1.2, C10.1, C11.1, C12.1, C13.1, C14.1, C15.1, C16.1, C17.1, C18.1, C19.1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
- removed net GND1: AUDIO1.SLEEVE, C37.2, C38.1, C39.1, C40.1, C41.1, C42.1, C43.1, C44.1, C45.1, C46.1, C47.1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
- removed net GND2: AUDIO2.SLEEVE, C100.2, C101.2, C105.2, C107.1, C108.1, C73.2, C74.1, C75.1, C76.1, C77.1, C78.1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
- removed net GND3: AUDIO3.SLEEVE, C109.2, C110.1, C111.1, C112.1, C113.1, C114.1, C115.1, C116.1, C117.1, C118.1, C119.1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
- removed net JOY_DOWN: JOY.2, U1.P5
- removed net JOY_DOWN1: JOY1.2, U8.P5
- removed net JOY_DOWN2: JOY2.2, U15.P5
- removed net JOY_DOWN3: JOY3.2, U22.P5
- removed net JOY_FIRE1: JOY.6, U1.P2
- removed net JOY_FIRE10: JOY3.6, U22.P2
- removed net JOY_FIRE11: JOY3.9, U22.P8
- removed net JOY_FIRE12: J15.1, U22.P39
- removed net JOY_FIRE2: JOY.9, U1.P8
- removed net JOY_FIRE3: J16.1, U1.P39
- removed net JOY_FIRE4: JOY1.6, U8.P2
- removed net JOY_FIRE5: JOY1.9, U8.P8
- removed net JOY_FIRE6: J4.1, U8.P39
- removed net JOY_FIRE7: JOY2.6, U15.P2
- removed net JOY_FIRE8: JOY2.9, U15.P8
- removed net JOY_FIRE9: J8.1, U15.P39
- removed net JOY_LEFT: JOY.3, U1.P6
- removed net JOY_LEFT1: JOY1.3, U8.P6
- removed net JOY_LEFT2: JOY2.3, U15.P6
- removed net JOY_LEFT3: JOY3.3, U22.P6
- removed net JOY_RIGHT: JOY.4, U1.P7
- removed net JOY_RIGHT1: JOY1.4, U8.P7
- removed net JOY_RIGHT2: JOY2.4, U15.P7
- removed net JOY_RIGHT3: JOY3.4, U22.P7
- removed net JOY_UP: JOY.1, U1.P1
- removed net JOY_UP1: JOY1.1, U8.P1
- removed net JOY_UP2: JOY2.1, U15.P1
- removed net JOY_UP3: JOY3.1, U22.P1
- removed net L-OUT: AUDIO.TIP, C34.2, RGB.9
- removed net L-OUT1: AUDIO1.TIP, C60.2, RGB1.9
- removed net L-OUT2: AUDIO2.TIP, C96.2, RGB2.9
- removed net L-OUT3: AUDIO3.TIP, C132.2, RGB3.9
- removed net LED: R6.2, U1.P11
- removed net LED1: R57.2, U8.P11
- removed net LED2: R89.2, U15.P11
- removed net LED3: R121.2, U22.P11
- removed net N$1: PS/2.6, R11.1
- removed net N$10: C3.1, C35.1, R23.1
- removed net N$100: C135.1, L11.1, U25.2
- removed net N$101: C137.1, L12.1, U26.2
- removed net N$102: C139.1, U27.7
- removed net N$103: C138.1, U27.6
- removed net N$104: C141.1, U27.3, Y7.2, Y8.2
- removed net N$105: D20.A, R120.1, Y8.1
- removed net N$106: D19.A, R119.2, Y7.1
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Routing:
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- removed copper zone on layer 1, net GND
- removed copper zone on layer 16, net GND
- removed copper zone on layer 1, net GND1
- removed copper zone on layer 16, net GND1
- removed copper zone on layer 1, net GND2
- removed copper zone on layer 16, net GND2
- removed copper zone on layer 1, net GND3
- removed copper zone on layer 16, net GND3
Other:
- board text removed: "(C)2015 ZX-Uno Team http://www.zxuno.com"
- board text removed: "1"
- board text removed: "AUDIO"
- board text removed: "C1"
- board text removed: "C10"
- board text removed: "C11"
- board text removed: "C12"
- board text removed: "C13"
- board text removed: "C14"
- board text removed: "C15"
- board text removed: "C16"
- board text removed: "C17"
- board text removed: "C18"
- board text removed: "C19"
- board text removed: "C2"
- board text removed: "C20"
- board text removed: "C21"
- board text removed: "C22"
- board text removed: "C23"
- board text removed: "C24"
- board text removed: "C25"
- board text removed: "C26"
- board text removed: "C27"
- board text removed: "C28"
- board text removed: "C29"
- board text removed: "C3"
- board text removed: "C30"
- board text removed: "C31"
- board text removed: "C32"
- board text removed: "C33"
- board text removed: "C34"
- board text removed: "C35"
- board text removed: "C36"
- board text removed: "C4"
- board text removed: "C5"
- board text removed: "C6"
- board text removed: "C7"
- board text removed: "C8"
- board text removed: "C9"
- board text removed: "CVBS"
- board text removed: "D1"
- board text removed: "D2"
- board text removed: "D3"
- board text removed: "D4"
- board text removed: "D5"
- board text removed: "EAR"
- board text removed: "J10"
- board text removed: "J11"
- board text removed: "J12"
- board text removed: "J16"
- board text removed: "JOY"
- board text removed: "JTAG"
- board text removed: "L1"
- board text removed: "L2"
- board text removed: "L3"
- board text removed: "PS/2"
- board text removed: "PWCON"
- board text removed: "PWUSB"
- board text removed: "R1"
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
